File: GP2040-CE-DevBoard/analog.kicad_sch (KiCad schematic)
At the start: 9 parts

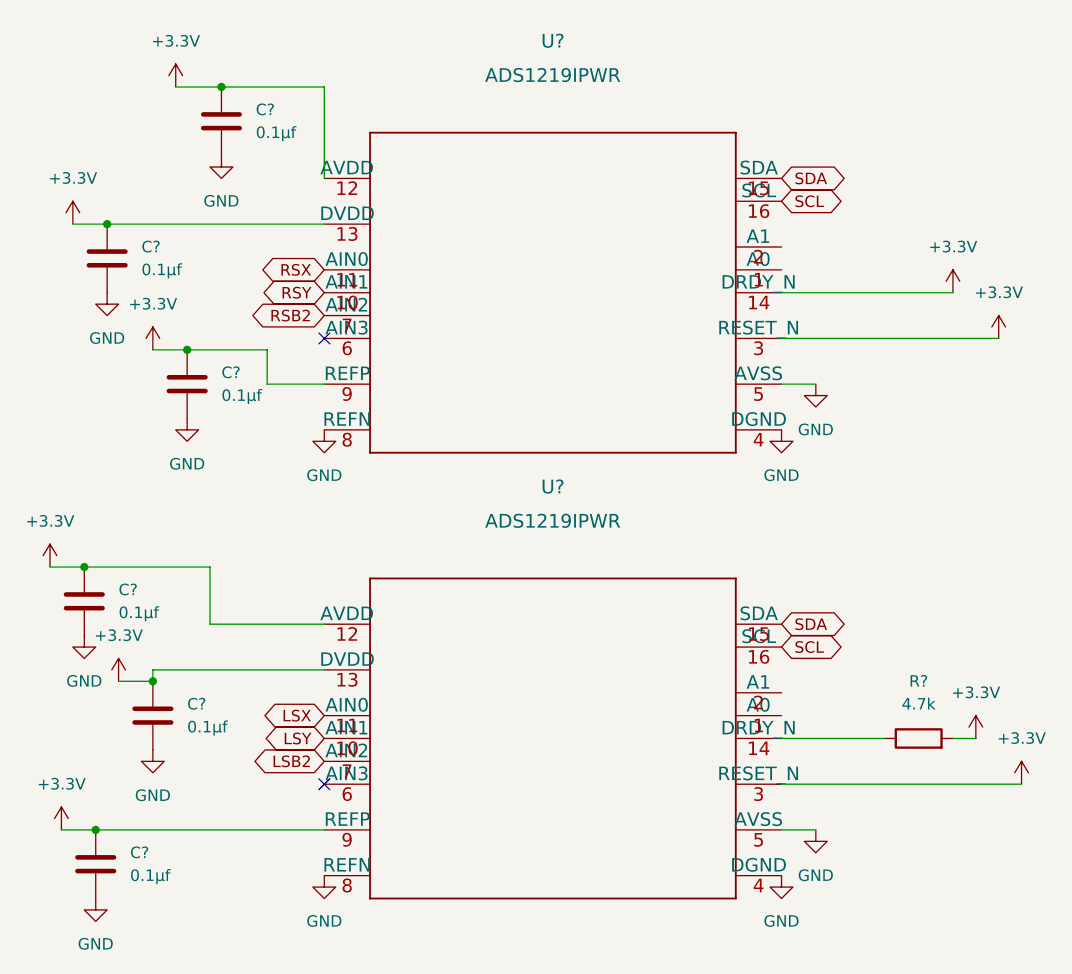
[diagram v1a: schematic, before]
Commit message: Schematic nearly complete, PCB started
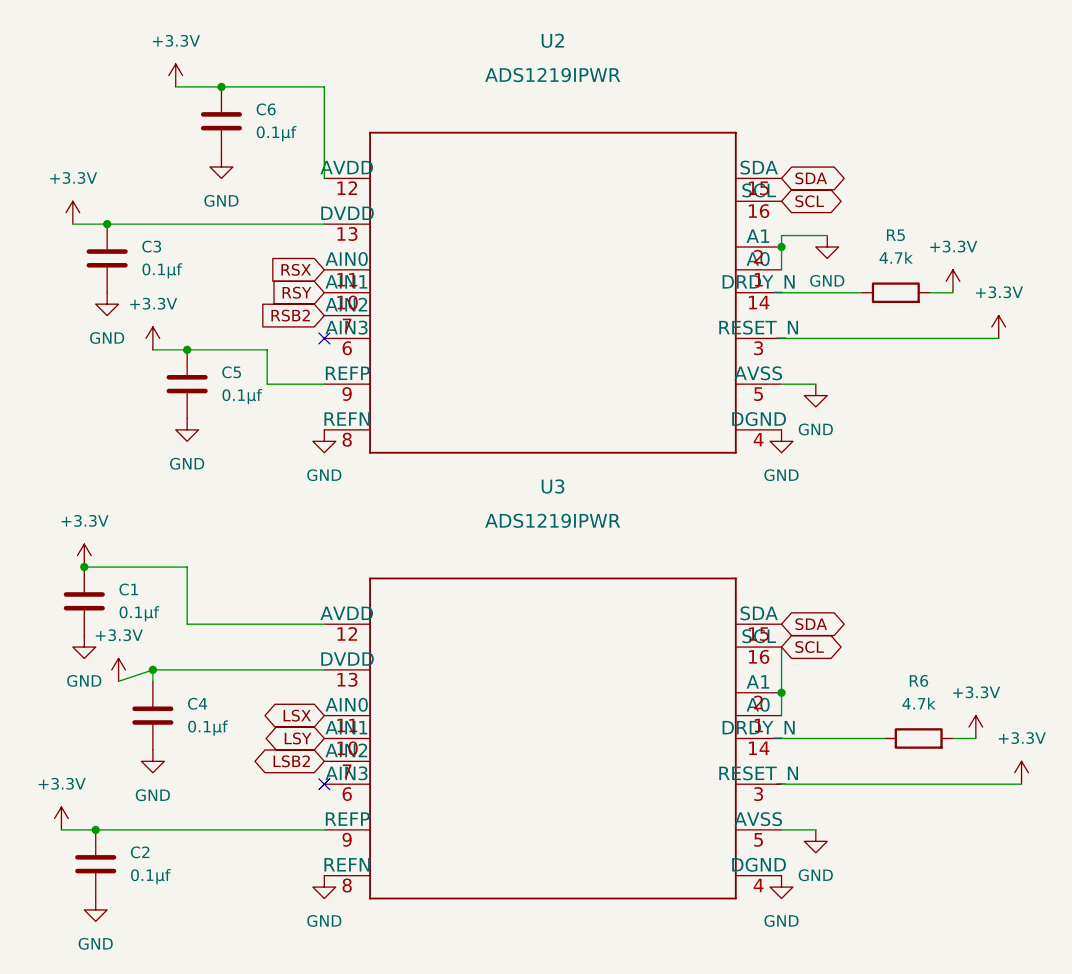
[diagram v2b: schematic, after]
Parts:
- added R5: 4.7k, Resistor_SMD:R_0805_2012Metric_Pad1.20x1.40mm_HandSolder, symbol Device:R
- gave numbers to parts that had none: 9
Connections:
- net +3V3: now also R5.2; no longer U2.14 (DRDY_N)
- net GND: now also U2.1 (A0), U2.2 (A1)
- net SCL: now also U3.1 (A0), U3.2 (A1)
- new net: R5.1, U2.14 (DRDY_N)

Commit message: Updating schema and PCB design
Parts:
- renumbered C6 to C4, C4 to C5, C5 to C6
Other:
- moved on the sheet: C4
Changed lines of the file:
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@@
   (junction (at 20.32 102.87) (diameter 0) (color 0 0 0 0)
   )
-  (junction (at 34.29 20.32) (diameter 0) (color 0 0 0 0)
-  )
   (junction (at 21.59 35.56) (diameter 0) (color 0 0 0 0)
   )
@@
   )
   (junction (at 19.05 73.66) (diameter 0) (color 0 0 0 0)
+  )
+  (junction (at 26.67 19.05) (diameter 0) (color 0 0 0 0)
   )
   (no_connect (at 45.72 48.26))
@@
     (stroke (width 0) (type default) (color 0 0 0 0))
   )
-  (wire (pts (xy 45.72 20.32) (xy 45.72 30.48))
-    (stroke (width 0) (type default) (color 0 0 0 0))
-  )
   (wire (pts (xy 16.51 102.87) (xy 20.32 102.87))
     (stroke (width 0) (type default) (color 0 0 0 0))
@@
     (stroke (width 0) (type default) (color 0 0 0 0))
   )
+  (wire (pts (xy 38.1 30.48) (xy 38.1 19.05))
+    (stroke (width 0) (type default) (color 0 0 0 0))
+  )
   (wire (pts (xy 39.37 49.53) (xy 30.48 49.53))
     (stroke (width 0) (type default) (color 0 0 0 0))
@@
     (stroke (width 0) (type default) (color 0 0 0 0))
   )
+  (wire (pts (xy 45.72 30.48) (xy 38.1 30.48))
+    (stroke (width 0) (type default) (color 0 0 0 0))
+  )
+  (wire (pts (xy 26.67 19.05) (xy 38.1 19.05))
+    (stroke (width 0) (type default) (color 0 0 0 0))
+  )
   (wire (pts (xy 45.72 80.01) (xy 30.48 80.01))
     (stroke (width 0) (type default) (color 0 0 0 0))
   )
-  (wire (pts (xy 29.21 20.32) (xy 34.29 20.32))
-    (stroke (width 0) (type default) (color 0 0 0 0))
-  )
   (wire (pts (xy 21.59 35.56) (xy 45.72 35.56))
     (stroke (width 0) (type default) (color 0 0 0 0))
@@
   )
   (wire (pts (xy 26.67 85.09) (xy 45.72 85.09))
-    (stroke (width 0) (type default) (color 0 0 0 0))
-  )
-  (wire (pts (xy 34.29 20.32) (xy 45.72 20.32))
     (stroke (width 0) (type default) (color 0 0 0 0))
   )
@@
       (effects (font (size 1.27 1.27)) (justify right) hide)
     )
+  )
+  (symbol (lib_id "power:+3.3V") (at 26.67 19.05 0) (unit 1)
+    (in_bom yes) (on_board yes) (fields_autoplaced)
+    (property "Reference" "#PWR029" (id 0) (at 26.67 22.86 0)
+      (effects (font (size 1.27 1.27)) hide)
+    )
+    (property "Value" "+3.3V" (id 1) (at 26.67 13.97 0))
+    (property "Footprint" "" (id 2) (at 26.67 19.05 0)
+      (effects (font (size 1.27 1.27)) hide)
+    )
+    (property "Datasheet" "" (id 3) (at 26.67 19.05 0)
+      (effects (font (size 1.27 1.27)) hide)
+    )
+    (pin "1")
   )
   (symbol (lib_id "power:+3.3V") (at 17.78 35.56 0) (unit 1)
@@
     (pin "2")
   )
-  (symbol (lib_id "power:+3.3V") (at 29.21 20.32 0) (unit 1)
-    (in_bom yes) (on_board yes) (fields_autoplaced)
-    (property "Reference" "#PWR031" (id 0) (at 29.21 24.13 0)
-      (effects (font (size 1.27 1.27)) hide)
-    )
-    (property "Value" "+3.3V" (id 1) (at 29.21 15.24 0))
-    (property "Footprint" "" (id 2) (at 29.21 20.32 0)
-      (effects (font (size 1.27 1.27)) hide)
-    )
-    (property "Datasheet" "" (id 3) (at 29.21 20.32 0)
-      (effects (font (size 1.27 1.27)) hide)
-    )
-    (pin "1")
-  )
   (symbol (lib_id "power:+3.3V") (at 16.51 102.87 0) (unit 1)
     (in_bom yes) (on_board yes) (fields_autoplaced)
@@
   (symbol (lib_id "power:+3.3V") (at 26.67 49.53 0) (unit 1)
     (in_bom yes) (on_board yes) (fields_autoplaced)
-    (property "Reference" "#PWR029" (id 0) (at 26.67 53.34 0)
+    (property "Reference" "#PWR031" (id 0) (at 26.67 53.34 0)
       (effects (font (size 1.27 1.27)) hide)
     )
@@
   (symbol (lib_id "power:GND") (at 30.48 57.15 0) (unit 1)
     (in_bom yes) (on_board yes) (fields_autoplaced)
-    (property "Reference" "#PWR032" (id 0) (at 30.48 63.5 0)
+    (property "Reference" "#PWR033" (id 0) (at 30.48 63.5 0)
       (effects (font (size 1.27 1.27)) hide)
     )
@@
     (pin "1")
   )
-  (symbol (lib_id "power:GND") (at 34.29 27.94 0) (unit 1)
-    (in_bom yes) (on_board yes) (fields_autoplaced)
-    (property "Reference" "#PWR033" (id 0) (at 34.29 34.29 0)
-      (effects (font (size 1.27 1.27)) hide)
-    )
-    (property "Value" "GND" (id 1) (at 34.29 33.02 0))
-    (property "Footprint" "" (id 2) (at 34.29 27.94 0)
-      (effects (font (size 1.27 1.27)) hide)
-    )
-    (property "Datasheet" "" (id 3) (at 34.29 27.94 0)
+  (symbol (lib_id "power:GND") (at 26.67 26.67 0) (unit 1)
+    (in_bom yes) (on_board yes) (fields_autoplaced)
+    (property "Reference" "#PWR030" (id 0) (at 26.67 33.02 0)
+      (effects (font (size 1.27 1.27)) hide)
+    )
+    (property "Value" "GND" (id 1) (at 26.67 31.75 0))
+    (property "Footprint" "" (id 2) (at 26.67 26.67 0)
+      (effects (font (size 1.27 1.27)) hide)
+    )
+    (property "Datasheet" "" (id 3) (at 26.67 26.67 0)
       (effects (font (size 1.27 1.27)) hide)
     )
@@
   (symbol (lib_id "Device:C") (at 30.48 53.34 0) (unit 1)
     (in_bom yes) (on_board yes) (fields_autoplaced)
-    (property "Reference" "C5" (id 0) (at 34.29 52.0699 0)
+    (property "Reference" "C6" (id 0) (at 34.29 52.0699 0)
       (effects (font (size 1.27 1.27)) (justify left))
     )
@@
   (symbol (lib_id "Device:C") (at 26.67 90.17 0) (unit 1)
     (in_bom yes) (on_board yes) (fields_autoplaced)
-    (property "Reference" "C4" (id 0) (at 30.48 88.8999 0)
+    (property "Reference" "C5" (id 0) (at 30.48 88.8999 0)
       (effects (font (size 1.27 1.27)) (justify left))
     )
@@
     (pin "2")
   )
-  (symbol (lib_id "Device:C") (at 34.29 24.13 0) (unit 1)
-    (in_bom yes) (on_board yes) (fields_autoplaced)
-    (property "Reference" "C6" (id 0) (at 38.1 22.8599 0)
-      (effects (font (size 1.27 1.27)) (justify left))
-    )
-    (property "Value" "0.1μf" (id 1) (at 38.1 25.3999 0)
-      (effects (font (size 1.27 1.27)) (justify left))
-    )
-    (property "Footprint" "Capacitor_SMD:C_0805_2012Metric_Pad1.18x1.45mm_HandSolder" (id 2) (at 35.2552 27.94 0)
-      (effects (font (size 1.27 1.27)) hide)
-    )
-    (property "Datasheet" "~" (id 3) (at 34.29 24.13 0)
+  (symbol (lib_id "Device:C") (at 26.67 22.86 0) (unit 1)
+    (in_bom yes) (on_board yes) (fields_autoplaced)
+    (property "Reference" "C4" (id 0) (at 30.48 21.5899 0)
+      (effects (font (size 1.27 1.27)) (justify left))
+    )
+    (property "Value" "0.1μf" (id 1) (at 30.48 24.1299 0)
+      (effects (font (size 1.27 1.27)) (justify left))
+    )
+    (property "Footprint" "Capacitor_SMD:C_0805_2012Metric_Pad1.18x1.45mm_HandSolder" (id 2) (at 27.6352 26.67 0)
+      (effects (font (size 1.27 1.27)) hide)
+    )
+    (property "Datasheet" "~" (id 3) (at 26.67 22.86 0)
       (effects (font (size 1.27 1.27)) hide)
     )
@@
   (symbol (lib_id "power:GND") (at 26.67 93.98 0) (unit 1)
     (in_bom yes) (on_board yes) (fields_autoplaced)
-    (property "Reference" "#PWR030" (id 0) (at 26.67 100.33 0)
-      (effects (font (size 1.27 1.27)) hide)
-    )
+    (property "Reference" "#PWR032" (id 0) (at 26.67 100.33 0)
+      (effects (font (size 1.27 1.27)) hide)
+    )

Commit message: a lot of Silkscreen work
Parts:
- C1, C2, C3, C4, C5, C6: footprint Capacitor_SMD:C_0805_2012Metric_Pad1.18x1.45mm_HandSolder -> OpenStick:C_0805_2012Metric_Pad1.18x1.45mm_HandSolder
- R5, R6: footprint Resistor_SMD:R_0805_2012Metric_Pad1.20x1.40mm_HandSolder -> OpenStick:R_0805_2012Metric_Pad1.20x1.40mm_HandSolder
- U2, U3: footprint ul_ADS1219IPWR:ADS1219IPWR -> OpenStick:ADS1219IPWR
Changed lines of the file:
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@@
       (effects (font (size 1.524 1.524)))
     )
-    (property "Footprint" "ul_ADS1219IPWR:ADS1219IPWR" (id 2) (at 71.12 94.234 0)
+    (property "Footprint" "OpenStick:ADS1219IPWR" (id 2) (at 71.12 94.234 0)
       (effects (font (size 1.524 1.524)) hide)
     )
@@
       (effects (font (size 1.27 1.27)) (justify left))
     )
-    (property "Footprint" "Capacitor_SMD:C_0805_2012Metric_Pad1.18x1.45mm_HandSolder" (id 2) (at 22.5552 43.18 0)
+    (property "Footprint" "OpenStick:C_0805_2012Metric_Pad1.18x1.45mm_HandSolder" (id 2) (at 22.5552 43.18 0)
       (effects (font (size 1.27 1.27)) hide)
     )
@@
       (effects (font (size 1.27 1.27)) (justify left))
     )
-    (property "Footprint" "Capacitor_SMD:C_0805_2012Metric_Pad1.18x1.45mm_HandSolder" (id 2) (at 20.0152 81.28 0)
+    (property "Footprint" "OpenStick:C_0805_2012Metric_Pad1.18x1.45mm_HandSolder" (id 2) (at 20.0152 81.28 0)
       (effects (font (size 1.27 1.27)) hide)
     )
@@
       (effects (font (size 1.27 1.27)) (justify left))
     )
-    (property "Footprint" "Capacitor_SMD:C_0805_2012Metric_Pad1.18x1.45mm_HandSolder" (id 2) (at 21.2852 110.49 0)
+    (property "Footprint" "OpenStick:C_0805_2012Metric_Pad1.18x1.45mm_HandSolder" (id 2) (at 21.2852 110.49 0)
       (effects (font (size 1.27 1.27)) hide)
     )
@@
       (effects (font (size 1.524 1.524)))
     )
-    (property "Footprint" "ul_ADS1219IPWR:ADS1219IPWR" (id 2) (at 71.12 44.704 0)
+    (property "Footprint" "OpenStick:ADS1219IPWR" (id 2) (at 71.12 44.704 0)
       (effects (font (size 1.524 1.524)) hide)
     )
@@
       (effects (font (size 1.27 1.27)) (justify left))
     )
-    (property "Footprint" "Capacitor_SMD:C_0805_2012Metric_Pad1.18x1.45mm_HandSolder" (id 2) (at 31.4452 57.15 0)
+    (property "Footprint" "OpenStick:C_0805_2012Metric_Pad1.18x1.45mm_HandSolder" (id 2) (at 31.4452 57.15 0)
       (effects (font (size 1.27 1.27)) hide)
     )
@@
       (effects (font (size 1.27 1.27)) (justify left))
     )
-    (property "Footprint" "Capacitor_SMD:C_0805_2012Metric_Pad1.18x1.45mm_HandSolder" (id 2) (at 27.6352 93.98 0)
+    (property "Footprint" "OpenStick:C_0805_2012Metric_Pad1.18x1.45mm_HandSolder" (id 2) (at 27.6352 93.98 0)
       (effects (font (size 1.27 1.27)) hide)
     )
@@
     (property "Reference" "R5" (id 0) (at 109.22 36.83 90))
     (property "Value" "4.7k" (id 1) (at 109.22 39.37 90))
-    (property "Footprint" "Resistor_SMD:R_0805_2012Metric_Pad1.20x1.40mm_HandSolder" (id 2) (at 109.22 44.958 90)
+    (property "Footprint" "OpenStick:R_0805_2012Metric_Pad1.20x1.40mm_HandSolder" (id 2) (at 109.22 44.958 90)
       (effects (font (size 1.27 1.27)) hide)
     )
@@
       (effects (font (size 1.27 1.27)) (justify left))
     )
-    (property "Footprint" "Capacitor_SMD:C_0805_2012Metric_Pad1.18x1.45mm_HandSolder" (id 2) (at 27.6352 26.67 0)
+    (property "Footprint" "OpenStick:C_0805_2012Metric_Pad1.18x1.45mm_HandSolder" (id 2) (at 27.6352 26.67 0)
       (effects (font (size 1.27 1.27)) hide)
     )
@@
     (property "Reference" "R6" (id 0) (at 111.76 86.36 90))
     (property "Value" "4.7k" (id 1) (at 111.76 88.9 90))
-    (property "Footprint" "Resistor_SMD:R_0805_2012Metric_Pad1.20x1.40mm_HandSolder" (id 2) (at 111.76 94.488 90)
-      (effects (font (size 1.27 1.27)) hide)
-    )
+    (property "Footprint" "OpenStick:R_0805_2012Metric_Pad1.20x1.40mm_HandSolder" (id 2) (at 111.76 94.488 90)
+      (effects (font (size 1.27 1.27)) hide)
+    )
